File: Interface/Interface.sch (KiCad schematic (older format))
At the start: 3 parts, among them SW1 SW_SPST, U1 SN74LVC1T45

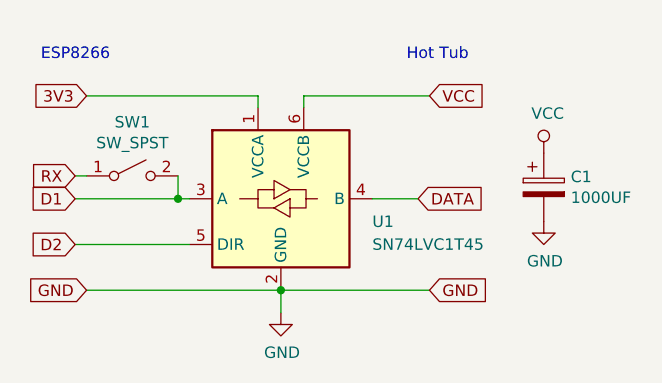
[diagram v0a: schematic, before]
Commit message: Updated schematic with missing vcc connections
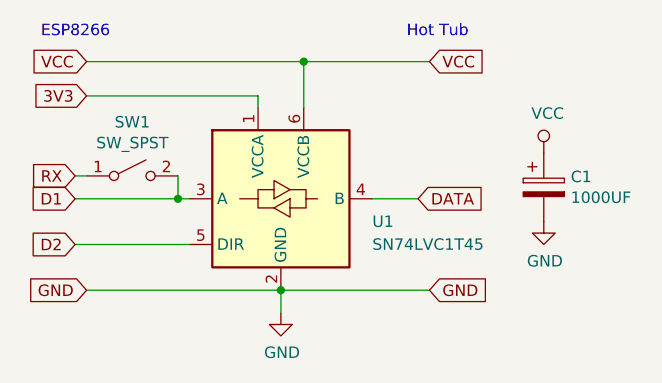
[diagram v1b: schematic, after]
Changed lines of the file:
@@
 $EndComp
-Wire Wire Line
-	5300 1550 5300 1500
 Wire Wire Line
 	5100 1550 5100 1500
@@
 Wire Wire Line
 	4350 1850 4300 1850
-Wire Wire Line
-	5300 1500 5850 1500
-Text GLabel 5850 1500 2    50   Input ~ 0
+Text GLabel 5850 1350 2    50   Input ~ 0
 VCC
 Text GLabel 4350 2350 0    50   Input ~ 0
 GND
-Text Notes 4150 1350 0    50   ~ 0
+Text Notes 4150 1250 0    50   ~ 0
 ESP8266
-Text Notes 5750 1350 0    50   ~ 0
+Text Notes 5750 1250 0    50   ~ 0
 Hot Tub
 Wire Wire Line
@@
 Wire Wire Line
 	4350 1500 5100 1500
+Text GLabel 4350 1350 0    50   Input ~ 0
+VCC
+Wire Wire Line
+	4350 1350 5300 1350
+Connection ~ 5300 1350
+Wire Wire Line
+	5300 1350 5850 1350
+Wire Wire Line
+	5300 1350 5300 1550
 $EndSCHEMATC
